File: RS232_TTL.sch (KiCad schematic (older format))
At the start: 6 parts, among them U6 ST3232E

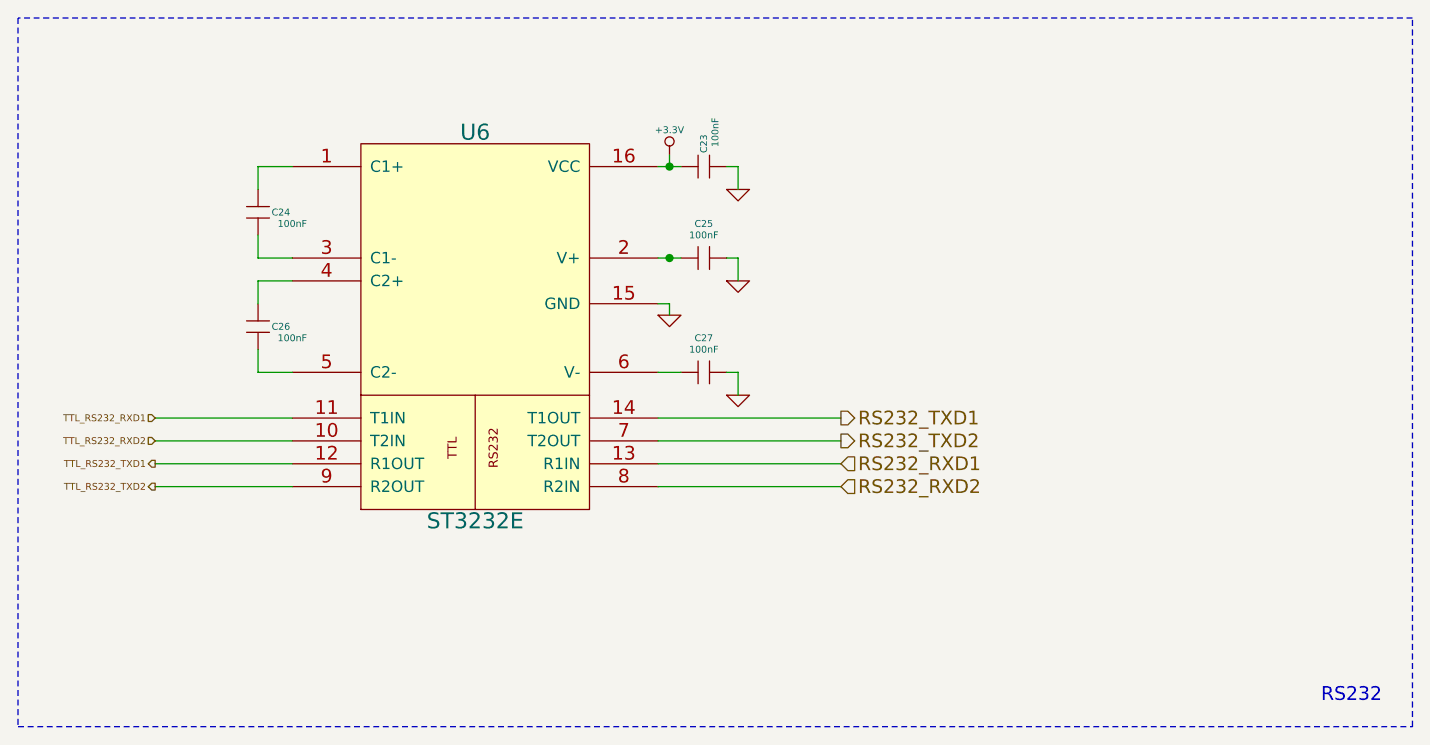
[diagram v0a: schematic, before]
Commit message: Max3232 -ok, Fuente ok, Buttons y Leds, OK. Fuente correinte OK, Falta Potenciometros y LM35.
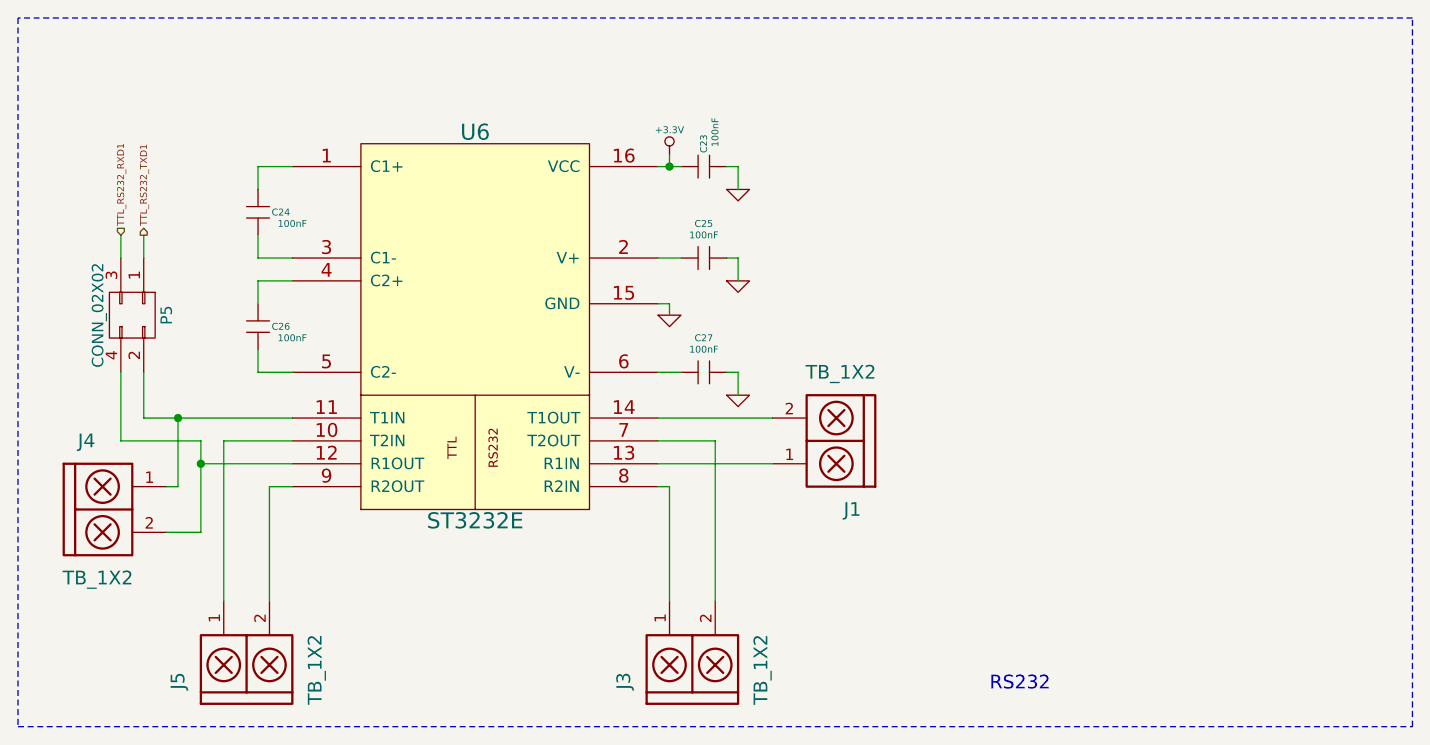
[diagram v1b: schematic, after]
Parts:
- added J1, J3, J4, J5: TB_1X2, symbol TB_1X2
- added P5: CONN_02X02, symbol CONN_02X02
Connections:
- net TTL_RS232_RXD1: now also P5.3 (P3); no longer U6.11 (T1IN)
- net TTL_RS232_TXD1: now also P5.1 (P1); no longer U6.12 (R1OUT)
- net RS232_RXD1: no longer names the net of U6.13 (R1IN)
- net RS232_RXD1: now also J1.1
- net RS232_RXD2: no longer names the net of U6.8 (R2IN)
- net RS232_RXD2: now also J3.1
- net RS232_TXD1: no longer names the net of U6.14 (T1OUT)
- net RS232_TXD1: now also J1.2
- net RS232_TXD2: no longer names the net of U6.7 (T2OUT)
- net RS232_TXD2: now also J3.2
- net TTL_RS232_RXD2: no longer names the net of U6.10 (T2IN)
- net TTL_RS232_RXD2: now also J5.1
- net TTL_RS232_TXD2: no longer names the net of U6.9 (R2OUT)
- net TTL_RS232_TXD2: now also J5.2
- new net: J4.1, P5.2 (P2), U6.11 (T1IN)
- new net: J4.2, P5.4 (P4), U6.12 (R1OUT)
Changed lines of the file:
@@
 $Descr A4 11693 8268
 encoding utf-8
-Sheet 2 4
+Sheet 2 6
 Title "CIAA RS485 - RS232 - CAN"
 Date "11 may 2015"
@@
 $EndComp
 $Comp
-L GND-RESCUE-ciaa-nxp #PWR095
+L GND-RESCUE-ciaa-nxp #PWR01
 U 1 1 52C5B356
 P 5950 3350
-F 0 "#PWR095" H 5950 3350 30  0001 C CNN
+F 0 "#PWR01" H 5950 3350 30  0001 C CNN
 F 1 "GND" H 5950 3280 30  0001 C CNN
 F 2 "" H 5950 3350 60  0000 C CNN
@@
 $EndComp
 $Comp
-L GND-RESCUE-ciaa-nxp #PWR096
+L GND-RESCUE-ciaa-nxp #PWR02
 U 1 1 52C5B357
 P 5950 3850
-F 0 "#PWR096" H 5950 3850 30  0001 C CNN
+F 0 "#PWR02" H 5950 3850 30  0001 C CNN
 F 1 "GND" H 5950 3780 30  0001 C CNN
 F 2 "" H 5950 3850 60  0000 C CNN
@@
 	1    0    0    -1
 $EndComp
-Text Notes 8500 5200 0    60   ~ 0
+Text Notes 7050 5150 0    60   ~ 0
 RS232
-Text HLabel 3400 3950 0    30   Input ~ 0
+Text HLabel 3250 3150 1    30   Input ~ 0
 TTL_RS232_RXD1
-Text HLabel 3400 4050 0    30   Input ~ 0
-TTL_RS232_RXD2
-Text HLabel 3400 4250 0    30   Output ~ 0
-TTL_RS232_TXD2
-Text HLabel 3400 4150 0    30   Output ~ 0
+Text HLabel 3350 3150 1    30   Output ~ 0
 TTL_RS232_TXD1
 $Comp
@@
 $EndComp
 $Comp
-L GND-RESCUE-ciaa-nxp #PWR0107
+L GND-RESCUE-ciaa-nxp #PWR03
 U 1 1 52C620B8
 P 5650 3500
-F 0 "#PWR0107" H 5650 3500 30  0001 C CNN
+F 0 "#PWR03" H 5650 3500 30  0001 C CNN
 F 1 "GND" H 5650 3430 30  0001 C CNN
 F 2 "" H 5650 3500 60  0000 C CNN
@@
 $EndComp
 $Comp
-L GND-RESCUE-ciaa-nxp #PWR0108
+L GND-RESCUE-ciaa-nxp #PWR04
 U 1 1 52C622EC
 P 5950 2950
-F 0 "#PWR0108" H 5950 2950 30  0001 C CNN
+F 0 "#PWR04" H 5950 2950 30  0001 C CNN
 F 1 "GND" H 5950 2880 30  0001 C CNN
 F 2 "" H 5950 2950 60  0000 C CNN
@@
 $EndComp
 $Comp
-L +3.3V-RESCUE-ciaa-nxp #PWR0110
+L +3.3V-RESCUE-ciaa-nxp #PWR05
 U 1 1 52E1F170
 P 5650 2800
-F 0 "#PWR0110" H 5650 2760 30  0001 C CNN
+F 0 "#PWR05" H 5650 2760 30  0001 C CNN
 F 1 "+3.3V" H 5650 2910 30  0000 C CNN
 F 2 "" H 5650 2800 60  0000 C CNN
@@
 Wire Wire Line
 	3850 3750 4000 3750
-Wire Wire Line
-	4000 3950 3400 3950
-Wire Wire Line
-	3400 4050 4000 4050
-Wire Wire Line
-	4000 4150 3400 4150
-Wire Wire Line
-	4000 4250 3400 4250
 Wire Notes Line
 	8900 5300 8900 2200
@@
 Wire Wire Line
 	5950 2850 5950 2950
-Connection ~ 5650 3250
 Wire Notes Line
 	2800 2200 2800 5300
-Wire Wire Line
-	5600 3950 6400 3950
-Wire Wire Line
-	5600 4050 6400 4050
-Wire Wire Line
-	5600 4150 6400 4150
-Wire Wire Line
-	5600 4250 6400 4250
-Text HLabel 6400 4150 2    60   Input ~ 0
-RS232_RXD1
-Text HLabel 6400 4050 2    60   Output ~ 0
-RS232_TXD2
-Text HLabel 6400 3950 2    60   Output ~ 0
-RS232_TXD1
-Text HLabel 6400 4250 2    60   Input ~ 0
-RS232_RXD2
+$Comp
+L TB_1X2 J1
+U 1 1 581961FA
+P 6450 4050
+F 0 "J1" H 6450 4350 60  0000 C CNN
+F 1 "TB_1X2" H 6500 3750 60  0000 C CNN
+F 2 "" H 6400 4100 60  0000 C CNN
+F 3 "" H 6400 4100 60  0000 C CNN
+	1    6450 4050
+	-1   0    0    1
+$EndComp
+Wire Wire Line
+	5600 4050 5850 4050
+$Comp
+L CONN_02X02 P5
+U 1 1 581970D4
+P 3300 3500
+F 0 "P5" H 3300 3650 50  0000 C CNN
+F 1 "CONN_02X02" H 3300 3350 50  0000 C CNN
+F 2 "" H 3300 2300 50  0000 C CNN
+F 3 "" H 3300 2300 50  0000 C CNN
+	1    3300 3500
+	0    1    1    0
+$EndComp
+$Comp
+L TB_1X2 J4
+U 1 1 5819740E
+P 3100 4350
+F 0 "J4" H 3100 4650 60  0000 C CNN
+F 1 "TB_1X2" H 3150 4050 60  0000 C CNN
+F 2 "" H 3050 4400 60  0000 C CNN
+F 3 "" H 3050 4400 60  0000 C CNN
+	1    3100 4350
+	1    0    0    -1
+$EndComp
+$Comp
+L TB_1X2 J5
+U 1 1 58197493
+P 3800 5100
+F 0 "J5" H 3800 5400 60  0000 C CNN
+F 1 "TB_1X2" H 3850 4800 60  0000 C CNN
+F 2 "" H 3750 5150 60  0000 C CNN
+F 3 "" H 3750 5150 60  0000 C CNN
+	1    3800 5100
+	0    -1   -1   0
+$EndComp
+Wire Wire Line
+	4000 3950 3350 3950
+Wire Wire Line
+	3350 3950 3350 3750
+Wire Wire Line
+	4000 4150 3600 4150
+Wire Wire Line
+	3600 4050 3600 4450
+Wire Wire Line
+	3600 4050 3250 4050
+Wire Wire Line
+	3250 4050 3250 3750
+Wire Wire Line
+	3450 4250 3500 4250
+Wire Wire Line
+	3500 4250 3500 3950
+Connection ~ 3500 3950
+Wire Wire Line
+	3600 4450 3450 4450
+Connection ~ 3600 4150
+Wire Wire Line
+	4000 4250 3900 4250
+Wire Wire Line
+	3900 4250 3900 4750
+Wire Wire Line
+	3700 4750 3700 4050
+Wire Wire Line
+	3250 3150 3250 3250
+Wire Wire Line
+	3350 3150 3350 3250
+$Comp
+L TB_1X2 J3
+U 1 1 5819888F
+P 5750 5100
+F 0 "J3" H 5750 5400 60  0000 C CNN
+F 1 "TB_1X2" H 5800 4800 60  0000 C CNN
+F 2 "" H 5700 5150 60  0000 C CNN
+F 3 "" H 5700 5150 60  0000 C CNN
+	1    5750 5100
+	0    -1   -1   0
+$EndComp
+Wire Wire Line
+	5650 4250 5650 4750
+Wire Wire Line
+	5850 4050 5850 4750
+Wire Wire Line
+	5600 4150 6100 4150
+Wire Wire Line
+	6100 3950 5600 3950
+Wire Wire Line
+	3700 4050 4000 4050
+Wire Wire Line
+	5600 4250 5650 4250
 $EndSCHEMATC

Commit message: Arreglo Max3232_ok, Fuente_ok, Buttons&Leds, OK.Fuente correinte OK, Potenciometros OK y LM35 OK.
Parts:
- renumbered C24 to C1, C26 to C2, C23 to C3, C25 to C4, C27 to C5, J4 to J1, J5 to J2, J1 to J4, P5 to P1, U6 to U1
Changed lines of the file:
@@
 EESchema Schematic File Version 2
-LIBS:ciaa-nxp-rescue
-LIBS:power
-LIBS:device
-LIBS:transistors
-LIBS:conn
-LIBS:linear
-LIBS:regul
-LIBS:74xx
-LIBS:cmos4000
-LIBS:adc-dac
-LIBS:memory
-LIBS:xilinx
-LIBS:microcontrollers
-LIBS:dsp
-LIBS:microchip
-LIBS:analog_switches
-LIBS:motorola
-LIBS:texas
-LIBS:intel
-LIBS:audio
-LIBS:interface
-LIBS:digital-audio
-LIBS:philips
-LIBS:display
-LIBS:cypress
-LIBS:siliconi
-LIBS:opto
-LIBS:atmel
-LIBS:contrib
-LIBS:valves
+LIBS:sensors
 LIBS:74LVC1G04GW
+LIBS:93CXX
+LIBS:BLM15HG6015N1D
+LIBS:FT2232H
+LIBS:IS42S16400F
+LIBS:LPC4337JBD144
+LIBS:MIC2025
+LIBS:PBSS5240
+LIBS:PRTR5V0U2X
+LIBS:PS2805
+LIBS:SCHA5B0200
+LIBS:Si50x
+LIBS:TJA1040
+LIBS:TXB0108
+LIBS:Transil_diode
 LIBS:amesser-ad
 LIBS:amesser-cmos4000
@@
 LIBS:audio-vlsi
 LIBS:bat54_c
-LIBS:BLM15HG6015N1D
+LIBS:capteurs
+LIBS:fqt13n06l
 LIBS:g5v2
 LIBS:lm2596
+LIBS:mcp1415
+LIBS:mcp1416
 LIBS:mcu-nxp
 LIBS:mcu-st
-LIBS:MIC2025
+LIBS:my_lab
 LIBS:net-phy
 LIBS:nsi50010yt1g
-LIBS:PRTR5V0U2X
+LIBS:pbss5240xf
 LIBS:regulators
 LIBS:rs485_rs232_can
 LIBS:s25fl032p0xmfi013
-LIBS:SCHA5B0200
-LIBS:Si50x
-LIBS:Transil_diode
+LIBS:sw_push
+LIBS:tvs
 LIBS:w_device
-LIBS:LPC4337JBD144
-LIBS:IS42S16400F
-LIBS:TXB0108
-LIBS:FT2232H
-LIBS:93CXX
-LIBS:TJA1040
-LIBS:tvs
-LIBS:PBSS5240
-LIBS:pbss5240xf
-LIBS:sw_push
-LIBS:mcp1416
-LIBS:fqt13n06l
+LIBS:74xgxx
+LIBS:74xx
+LIBS:Altera
+LIBS:ESD_Protection
+LIBS:Lattice
+LIBS:Oscillators
+LIBS:Power_Management
+LIBS:Worldsemi
+LIBS:Xicor
+LIBS:Zilog
+LIBS:ac-dc
+LIBS:actel
+LIBS:adc-dac
+LIBS:analog_devices
+LIBS:analog_switches
+LIBS:atmel
+LIBS:audio
+LIBS:brooktre
+LIBS:cmos4000
+LIBS:cmos_ieee
+LIBS:conn
+LIBS:contrib
+LIBS:cypress
+LIBS:dc-dc
+LIBS:device
+LIBS:digital-audio
+LIBS:diode
+LIBS:display
+LIBS:dsp
+LIBS:elec-unifil
+LIBS:ftdi
+LIBS:gennum
+LIBS:graphic
+LIBS:hc11
+LIBS:intel
+LIBS:interface
+LIBS:ir
+LIBS:linear
+LIBS:logo
+LIBS:maxim
+LIBS:memory
+LIBS:microchip
+LIBS:microchip_dspic33dsc
+LIBS:microchip_pic10mcu
+LIBS:microchip_pic12mcu
+LIBS:microchip_pic16mcu
+LIBS:microchip_pic18mcu
+LIBS:microchip_pic32mcu
+LIBS:microcontrollers
+LIBS:motor_drivers
+LIBS:motorola
+LIBS:msp430
+LIBS:nordicsemi
+LIBS:nxp_armmcu
+LIBS:onsemi
+LIBS:opto
+LIBS:philips
+LIBS:power
+LIBS:powerint
+LIBS:pspice
+LIBS:references
+LIBS:regul
+LIBS:relays
+LIBS:rfcom
+LIBS:silabs
+LIBS:siliconi
+LIBS:stm8
+LIBS:stm32
+LIBS:supertex
+LIBS:switches
+LIBS:texas
+LIBS:transf
+LIBS:transistors
+LIBS:ttl_ieee
+LIBS:valves
+LIBS:video
+LIBS:xilinx
 LIBS:ciaa-nxp-cache
 EELAYER 25 0
@@
 $EndDescr
 $Comp
-L C_MINI C24
+L C_MINI C1
 U 1 1 52C5B352
 P 3850 3050
-F 0 "C24" V 3850 3150 30  0000 C CNN
+F 0 "C1" V 3850 3150 30  0000 C CNN
 F 1 "100nF" V 3900 3200 30  0000 C CNN
 F 2 "~" H 3850 3050 60  0000 C CNN
@@
 $EndComp
 $Comp
-L C_MINI C26
+L C_MINI C2
 U 1 1 52C5B353
 P 3850 3550
-F 0 "C26" V 3850 3650 30  0000 C CNN
+F 0 "C2" V 3850 3650 30  0000 C CNN
 F 1 "100nF" V 3900 3700 30  0000 C CNN
 F 2 "~" H 3850 3550 60  0000 C CNN
@@
 $EndComp
 $Comp
-L C_MINI C25
+L C_MINI C4
 U 1 1 52C5B354
 P 5800 3250
-F 0 "C25" H 5800 3400 30  0000 C CNN
+F 0 "C4" H 5800 3400 30  0000 C CNN
 F 1 "100nF" H 5800 3350 30  0000 C CNN
 F 2 "~" H 5800 3250 60  0000 C CNN
@@
 $EndComp
 $Comp
-L C_MINI C27
+L C_MINI C5
 U 1 1 52C5B355
 P 5800 3750
-F 0 "C27" H 5800 3900 30  0000 C CNN
+F 0 "C5" H 5800 3900 30  0000 C CNN
 F 1 "100nF" H 5800 3850 30  0000 C CNN
 F 2 "~" H 5800 3750 60  0000 C CNN
@@
 $EndComp
 $Comp
-L C_MINI C23
+L C_MINI C3
 U 1 1 52C5B359
 P 5800 2850
-F 0 "C23" V 5800 2950 30  0000 C CNN
+F 0 "C3" V 5800 2950 30  0000 C CNN
 F 1 "100nF" V 5850 3000 30  0000 C CNN
 F 2 "~" H 5800 2850 60  0000 C CNN
@@
 TTL_RS232_TXD1
 $Comp
-L ST3232E U6
+L ST3232E U1
 U 1 1 52C61C4D
 P 4800 3550
-F 0 "U6" H 4800 4400 70  0000 C CNN
+F 0 "U1" H 4800 4400 70  0000 C CNN
 F 1 "ST3232E" H 4800 2700 70  0000 C CNN
 F 2 "" H 4800 3550 60  0000 C CNN
@@
 	2800 2200 2800 5300
 $Comp
-L TB_1X2 J1
+L TB_1X2 J4
 U 1 1 581961FA
 P 6450 4050
-F 0 "J1" H 6450 4350 60  0000 C CNN
+F 0 "J4" H 6450 4350 60  0000 C CNN
 F 1 "TB_1X2" H 6500 3750 60  0000 C CNN
 F 2 "" H 6400 4100 60  0000 C CNN
@@
 	5600 4050 5850 4050
 $Comp
-L CONN_02X02 P5
+L CONN_02X02 P1
 U 1 1 581970D4
 P 3300 3500
-F 0 "P5" H 3300 3650 50  0000 C CNN
+F 0 "P1" H 3300 3650 50  0000 C CNN
 F 1 "CONN_02X02" H 3300 3350 50  0000 C CNN
 F 2 "" H 3300 2300 50  0000 C CNN
@@
 $EndComp
 $Comp
-L TB_1X2 J4
+L TB_1X2 J1
 U 1 1 5819740E
 P 3100 4350
-F 0 "J4" H 3100 4650 60  0000 C CNN
+F 0 "J1" H 3100 4650 60  0000 C CNN
 F 1 "TB_1X2" H 3150 4050 60  0000 C CNN
 F 2 "" H 3050 4400 60  0000 C CNN
@@
 $EndComp
 $Comp
-L TB_1X2 J5
+L TB_1X2 J2
 U 1 1 58197493
 P 3800 5100
-F 0 "J5" H 3800 5400 60  0000 C CNN
+F 0 "J2" H 3800 5400 60  0000 C CNN
 F 1 "TB_1X2" H 3850 4800 60  0000 C CNN
 F 2 "" H 3750 5150 60  0000 C CNN
